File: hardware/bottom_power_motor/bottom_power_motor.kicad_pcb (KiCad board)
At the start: 4 copper layers, 52 x 52 mm, 104 parts, among them J1 Power/Motor 6p, J2 J_STK_A, J3 J_STK_B, Q1 P-FET 40V 30A, U1 L78L12, U2 TPS54360, U2_CB 100n, U2_CO 47u, U2_CZ 3n3, U2_D 60V 3A, U2_L 10u, U2_RC 10k, U2_RH 53k6, U2_RL 10k2, U2_RT_R 100k, U3 TLV62569, U4 TPS54360, U4_CB 100n, U4_CO 22u, U4_CZ 3n3, U4_D 60V 3A, U4_L 33u, U4_RC 10k, U4_RH 68k1, U4_RL 10k0, U4_RT_R 100k

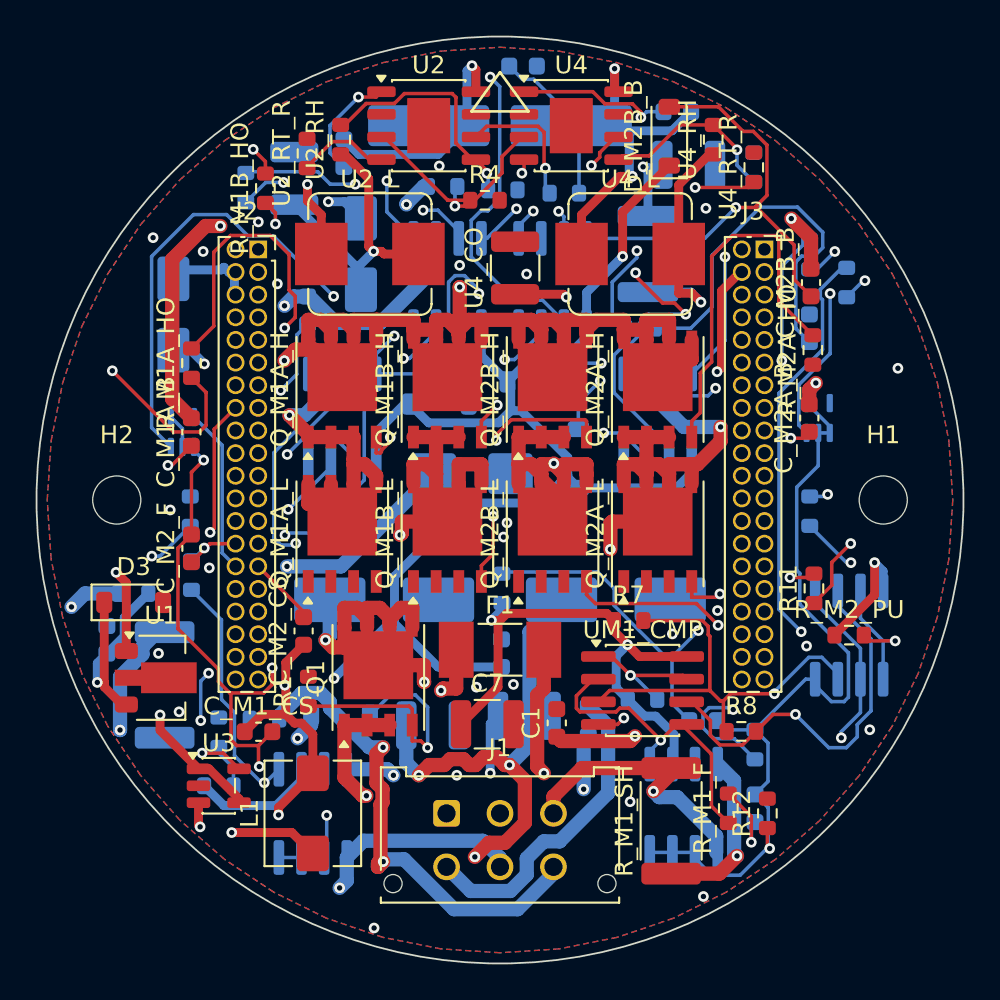
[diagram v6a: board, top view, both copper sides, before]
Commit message: Stack-Pinout v0.5: Tasten und I2C auf die Aussenreihe, Tasten auf beide Verbinder
Zwei Autorouter (1.9.0 und 2.3.0) und zwei Lagenzahlen hatten auf Top exakt
dieselben elf offenen Netze hinterlassen. Das ist kein Werkzeugproblem,
sondern die Pinbelegung.

BTN1..BTN4 lagen auf B26..B29 - vier benachbarten Kontakten der INNENreihe
des RECHTEN Verbinders. Ihre Taster sitzen aber in allen vier Ecken des
Top-Boards, zwei davon links. Zwei Bahnen mussten quer ueber ein Board mit
80 Steckkontakten im 1,27-mm-Raster, und alle vier zuerst aus der Innenreihe
heraus. I2C_SCL/SDA lagen ebenfalls innen.

Neu liegt jedes Tastennetz auf der AUSSENreihe des Verbinders, der seiner
Ecke am naechsten ist - von dort geht es direkt nach aussen und am Boardrand
entlang zum Taster:

  BTN1  B26 -> B1    aussen, y = -14,06   SW1 (+18 / -20)
  BTN2  B27 -> A2    aussen, y = -14,06   SW2 (-18 / -20)
  BTN3  B28 -> A40   aussen, y = +10,07   SW3 (-18 / +20)
  BTN4  B29 -> B39   aussen, y = +10,07   SW4 (+18 / +20)

  I2C_SCL  B6 -> B5  aussen
  I2C_SDA  B8 -> B7  aussen

Beide I2C-Teilnehmer auf Top - SHT4x und ToF - sitzen an der oberen Kante,
also dort, wo die neuen Pins liegen.

Die freigewordenen Kontakte B6, B8, B26..B29 werden PGND. Vier PGND-Pins sind
weggefallen (A2, A40, B1, B39); ueber beide Verbinder bleiben 25.

Alle drei Schaltplaene und Layouts neu erzeugt, Netzlistenvergleich bestanden,
keine Platzierungsfehler. Das Routing folgt.

Co-Authored-By: Claude Opus 5 (1M context) <noreply@anthropic.com>
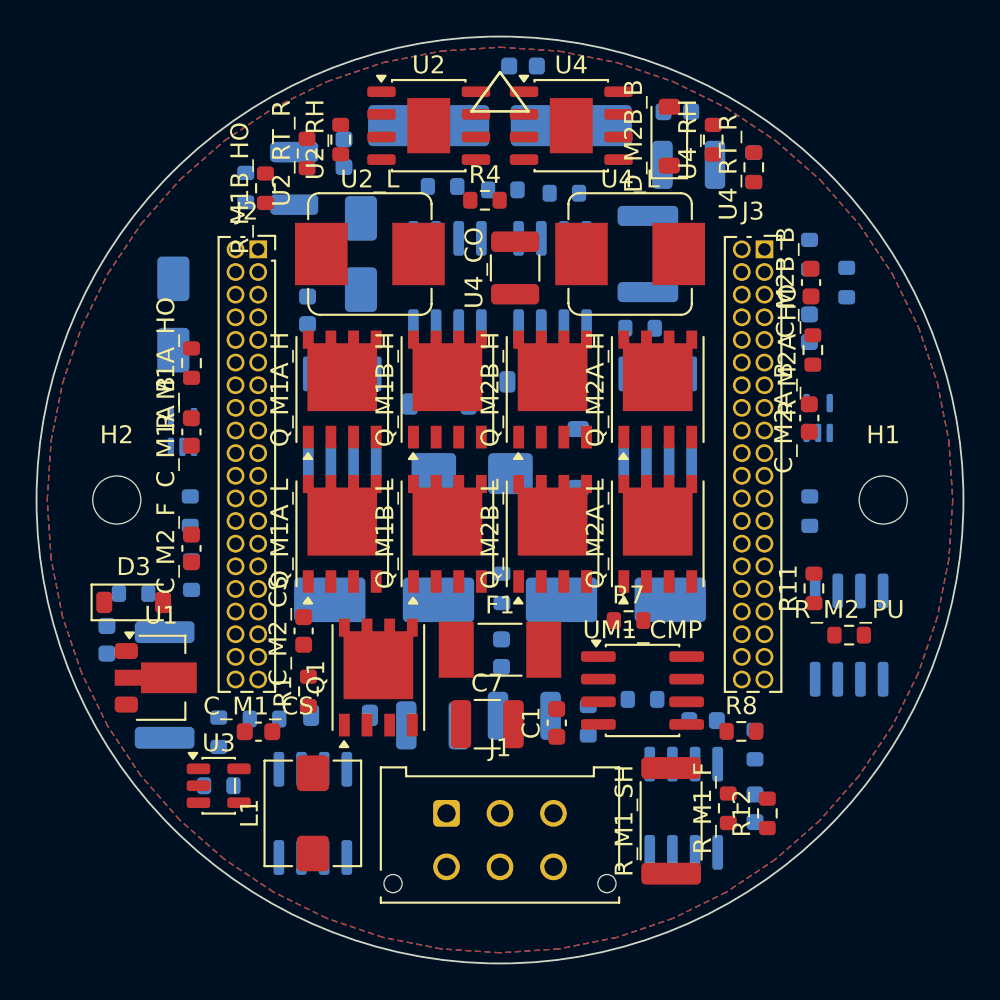
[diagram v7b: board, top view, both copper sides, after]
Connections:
- net USB_DN renamed RSV_A5
- net USB_DP renamed RSV_A3
- J2 pad 2: PGND -> BTN2
- J2 pad 40: PGND -> BTN3
- J3 pad 1: PGND -> BTN1
- J3 pad 26: BTN1 -> PGND
- J3 pad 27: BTN2 -> PGND
- J3 pad 28: BTN3 -> PGND
- J3 pad 29: BTN4 -> PGND
- J3 pad 39: PGND -> BTN4
- J3 pad 5: PGND -> I2C_SCL
- J3 pad 6: I2C_SCL -> PGND
- J3 pad 7: PGND -> I2C_SDA
- J3 pad 8: I2C_SDA -> PGND
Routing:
- net 24V_PROT: track 185.8 -> 0.00 mm, vias 11 -> 0
- net M1_SWA: track 161.0 -> 0.00 mm, vias 5 -> 0
- net 3V3_SYS: track 150.3 -> 0.00 mm, vias 7 -> 0
- net AGND: track 129.1 -> 0.00 mm, vias 6 -> 0
- net M2_SWA: track 98.2 -> 0.00 mm, vias 4 -> 0
- net 12V_GATE: track 94.4 -> 0.00 mm, vias 3 -> 0
- net TRIP_RST: track 91.4 -> 0.00 mm, vias 2 -> 0
- net M1A_HO_G: track 85.7 -> 0.00 mm, vias 5 -> 0
- net 5V_SYS: track 72.8 -> 0.00 mm, vias 3 -> 0
- net M1_SWB: track 69.8 -> 0.00 mm, vias 3 -> 0
- net M2B_HO_GT: track 64.4 -> 0.00 mm, vias 4 -> 0
- net M1A_LO_G: track 61.7 -> 0.00 mm, vias 5 -> 0
- net M2_ISNS: track 61.7 -> 0.00 mm, vias 2 -> 0
- net I_SENSE1: track 61.5 -> 0.00 mm, vias 5 -> 0
- net M1_SD: track 61.1 -> 0.00 mm, vias 4 -> 0
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
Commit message: Quadratischer Randkeepout: Top faellt von 11 auf 3 offene Netze
Der Kreisring war die Wand. Mit vier Balken entlang der Kanten statt eines
Annulus routet Freerouting auf Top durch:

              Segmente  Vias  offene Signale
  vorher         144      9        11
  jetzt          175     15         3   (3V3_SYS, I2C_SCL, I2C_SDA)

Alle vier Tastennetze und alle vier Stern-Netze sind jetzt verbunden. Damit
ist auch rueckwirkend klar, dass weder die Lagenzahl noch der Routerwechsel
noch das neue Pinout je eine Chance hatten - sie haben alle gegen dieselbe
unsichtbare Sperre gearbeitet.

DIE PROJEKTDATEIEN WERDEN BEIM SPEICHERN ZURUECKGESETZT. pcbnew.SaveBoard
legt die .kicad_pro mit KiCads Vorgaben neu an; die bewussten Entscheidungen
von gestern - 0,15 mm Abstand statt 0,2, ein Waermefallensteg statt zwei -
waren dadurch beim Neuerzeugen still verschwunden und erzeugten prompt wieder
Scheinverletzungen (Bottom 2 clearance, alle drei zusammen 34
starved_thermal). BoardBuilder.save() schreibt sie jetzt nach jedem Speichern
zurueck.

  starved_thermal  34 -> 0
  clearance         2 -> 1

STAND NACH gnd_connect

                Segmente  offene Signale  Masse-Inseln  Kupferfehler
  top_ui           175          3              1             1
  mid_logic        641          9             12             0
  bottom_power    1430          4             26             1

Der eine Kupferfehler auf Top ist der dokumentierte, absichtliche Ueberhang
der Klinkenbuchse ueber die Boardkante; der auf Bottom ein Haarriss von
0,1 statt 0,15 mm zwischen zwei Leistungsbahnen.

Co-Authored-By: Claude Opus 5 (1M context) <noreply@anthropic.com>
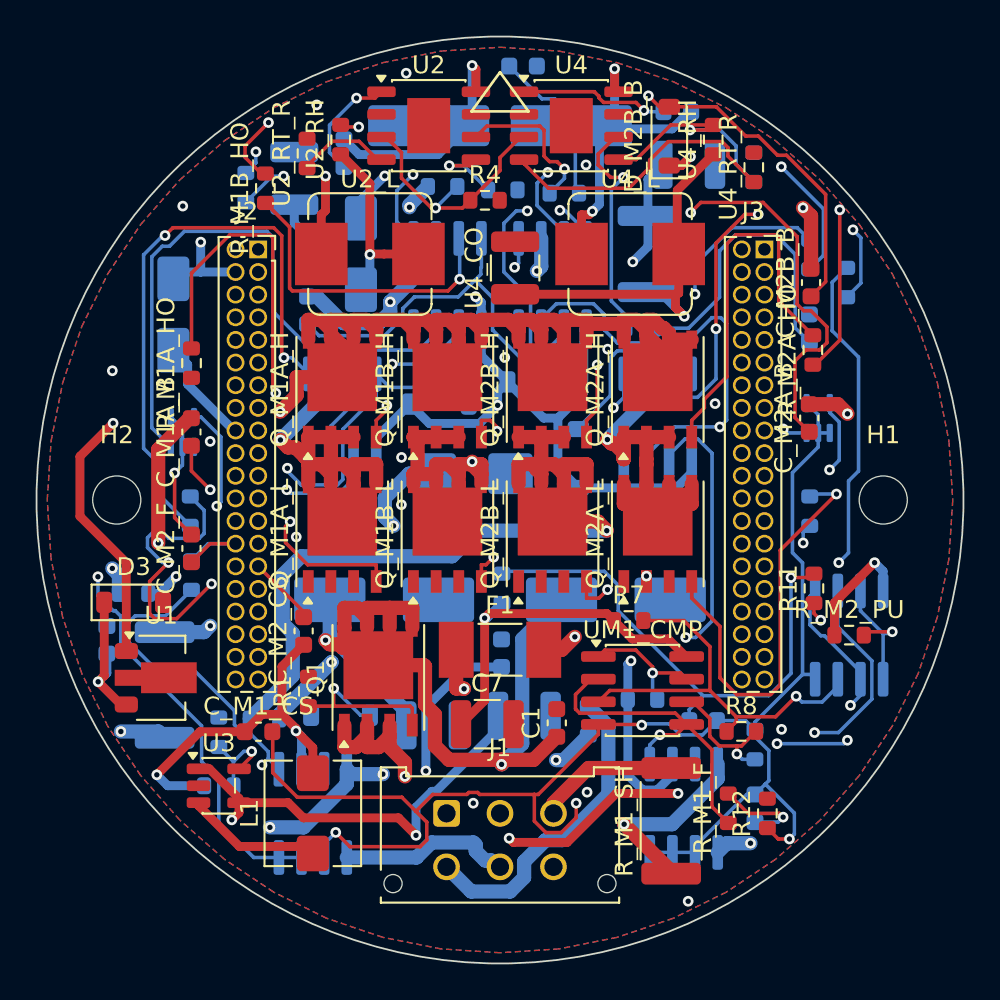
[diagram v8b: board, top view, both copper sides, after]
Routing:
- net 12V_GATE: track 0.00 -> 175.8 mm, vias 0 -> 13
- net 3V3_SYS: track 0.00 -> 172.8 mm, vias 0 -> 6
- net 24V_PROT: track 0.00 -> 165.3 mm, vias 0 -> 5
- net AGND: track 0.00 -> 157.8 mm, vias 0 -> 6
- net M2_INA: track 0.00 -> 124.0 mm, vias 0 -> 5
- net M1_SWA: track 0.00 -> 113.7 mm, vias 0 -> 3
- net M2_SWA: track 0.00 -> 109.2 mm, vias 0 -> 6
- net 5V_SYS: track 0.00 -> 86.5 mm, vias 0 -> 5
- net M2_SWB: track 0.00 -> 85.6 mm, vias 0 -> 3
- net M2_ISNS: track 0.00 -> 67.2 mm, vias 0 -> 2
- net HW_TRIP2: track 0.00 -> 59.6 mm, vias 0 -> 2
- net TRIP_RST: track 0.00 -> 59.4 mm, vias 0 -> 1
- net M1_SWB: track 0.00 -> 58.6 mm, vias 0 -> 3
- net M2_SD: track 0.00 -> 58.4 mm, vias 0 -> 2
- net I_SENSE1: track 0.00 -> 57.0 mm, vias 0 -> 2
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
